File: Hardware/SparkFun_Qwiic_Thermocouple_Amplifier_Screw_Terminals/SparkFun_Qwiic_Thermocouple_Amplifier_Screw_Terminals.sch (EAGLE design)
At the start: 26 parts, among them J1 PTH, U16 MCP9600-SMD

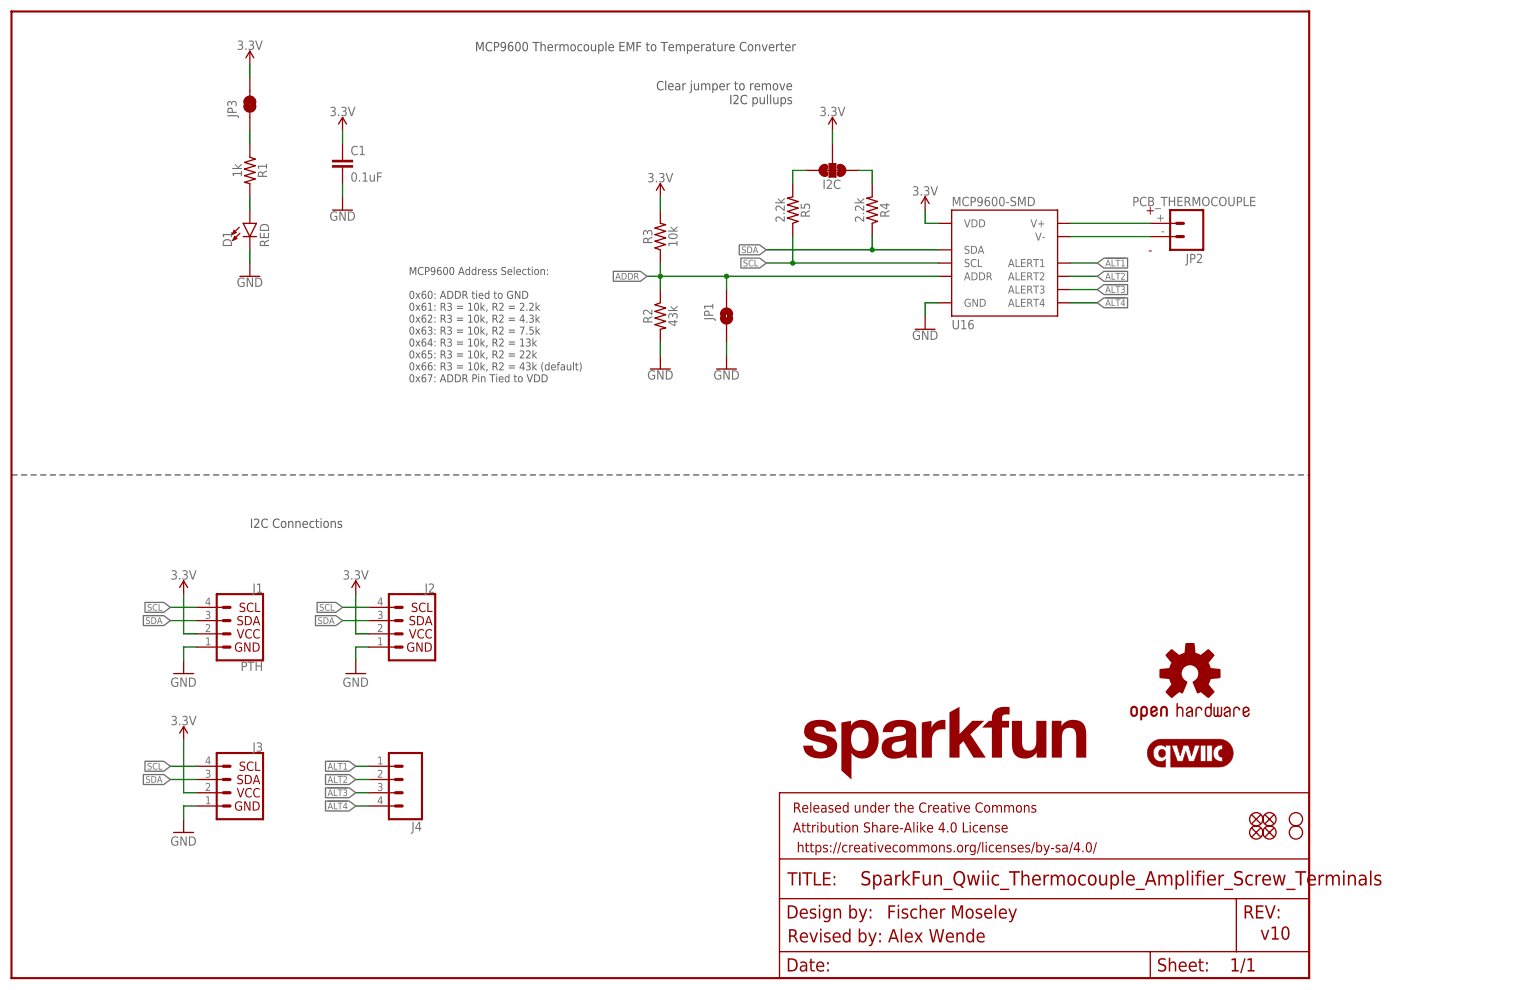
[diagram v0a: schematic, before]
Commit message: Added screw terminal board
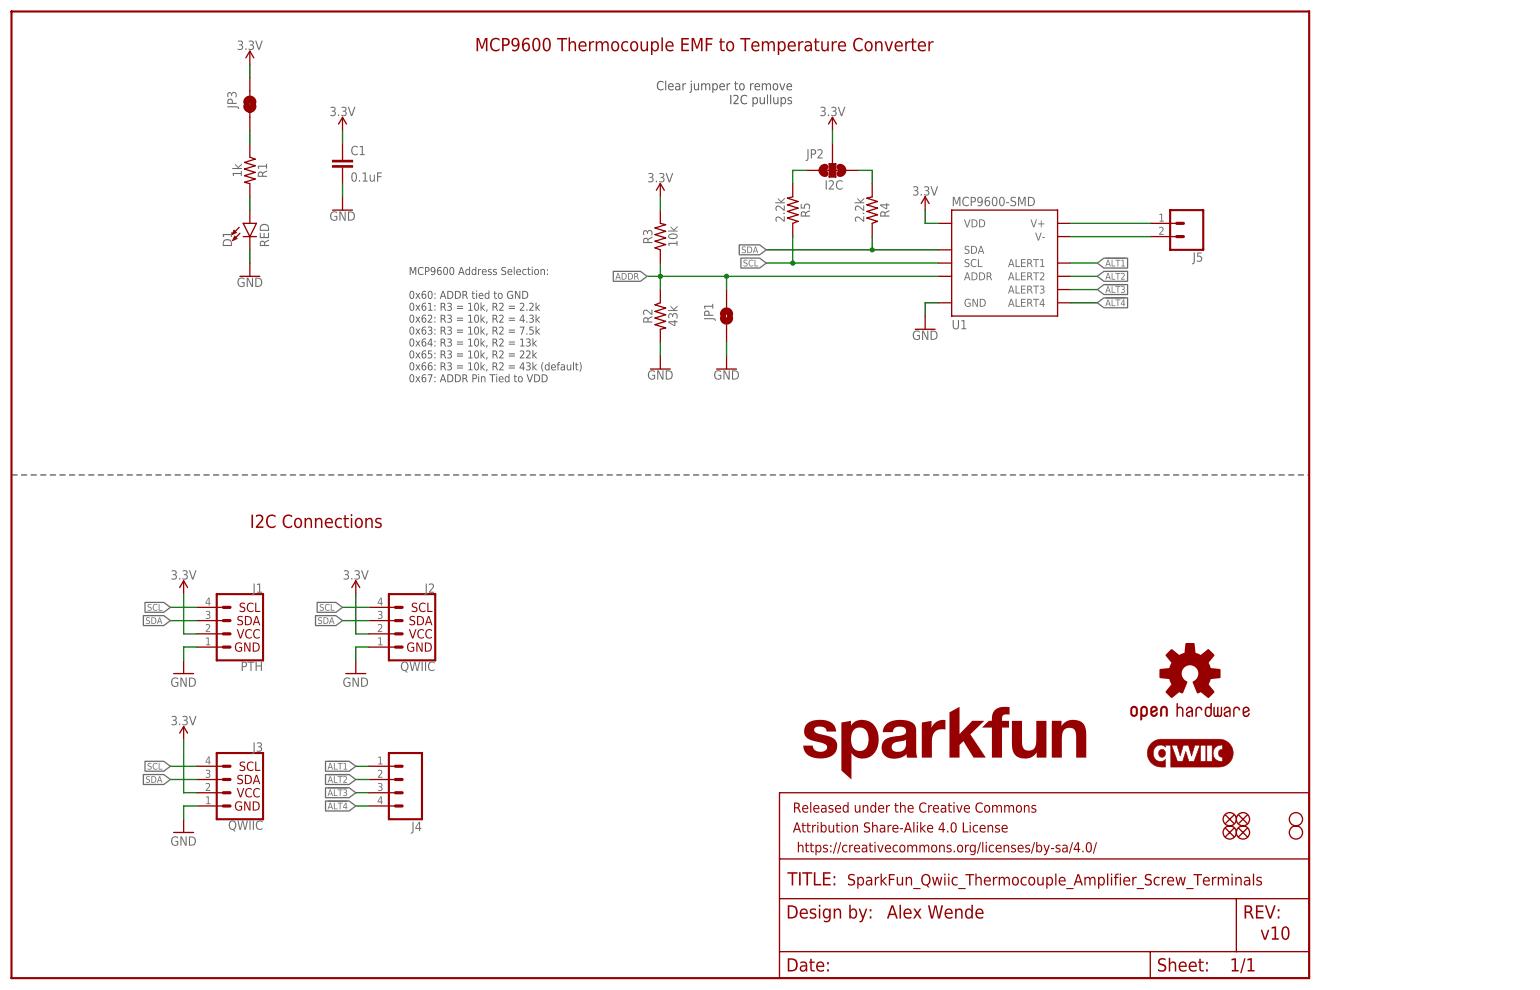
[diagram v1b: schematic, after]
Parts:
- removed I2C: JUMPER-SMT_3_2-NC_TRACE_SILK, SparkFun-Jumpers:JUMPER-SMT_3_2-NC_TRACE_SILK
- removed U16: MCP9600-SMD, MCP9600:MCP9600-SMD
- added J5: (no value), SparkFun-Connectors:CONN_023.5MM
- added U1: MCP9600-SMD, SparkFun-IC-Conversion:MCP9600-SMD
- FD1, FD2, FD3, FD4: value FIDUCIAL1X2 -> FIDUCIALUFIDUCIAL; device SparkFun-Aesthetics:FIDUCIAL1X2 -> SparkFun-Aesthetics:FIDUCIALUFIDUCIAL
- J1: device SparkX:I2C_STANDARD_NO_SILK -> SparkFun-Connectors:I2C_STANDARD_NO_SILK
- J2, J3: value (none) -> QWIIC
- JP2: value PCB_THERMOCOUPLE -> I2C; device MCP9600:PCB_THERMOCOUPLE -> SparkFun-Jumpers:JUMPER-SMT_3_2-NC_TRACE_SILK
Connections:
- net !ALT1: now also U1.ALERT1; no longer U16.ALERT1
- net !ALT2: now also U1.ALERT2; no longer U16.ALERT2
- net !ALT3: now also U1.ALERT3; no longer U16.ALERT3
- net !ALT4: now also U1.ALERT4; no longer U16.ALERT4
- net 3.3V: now also J1.2, JP2.2, JP3.1, U1.VDD; no longer I2C.2, J1.VCC, JP3.2, U16.VDD
- net ADDR: now also U1.ADDR; no longer U16.ADDR
- net GND: now also J1.1, U1.GND; no longer J1.GND, U16.GND
- net N$2: now also JP2.1; no longer I2C.1
- net N$3: now also JP2.3; no longer I2C.3
- net N$4: now also J5.1, U1.V+; no longer JP2G$1.+, U16.V+
- net N$5: now also J5.2, U1.V-; no longer JP2G$1.-, U16.V-
- net N$6: now also JP3.2; no longer JP3.1
- net SCL: now also J1.4, U1.SCL; no longer J1.SCL, U16.SCL
- net SDA: now also J1.3, U1.SDA; no longer J1.SDA, U16.SDA
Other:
- note added: "Alex Wende"
- note removed: "Fischer Moseley"
- note removed: "Revised by: Alex Wende"
- moved on the sheet: JP3

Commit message: Design review changes
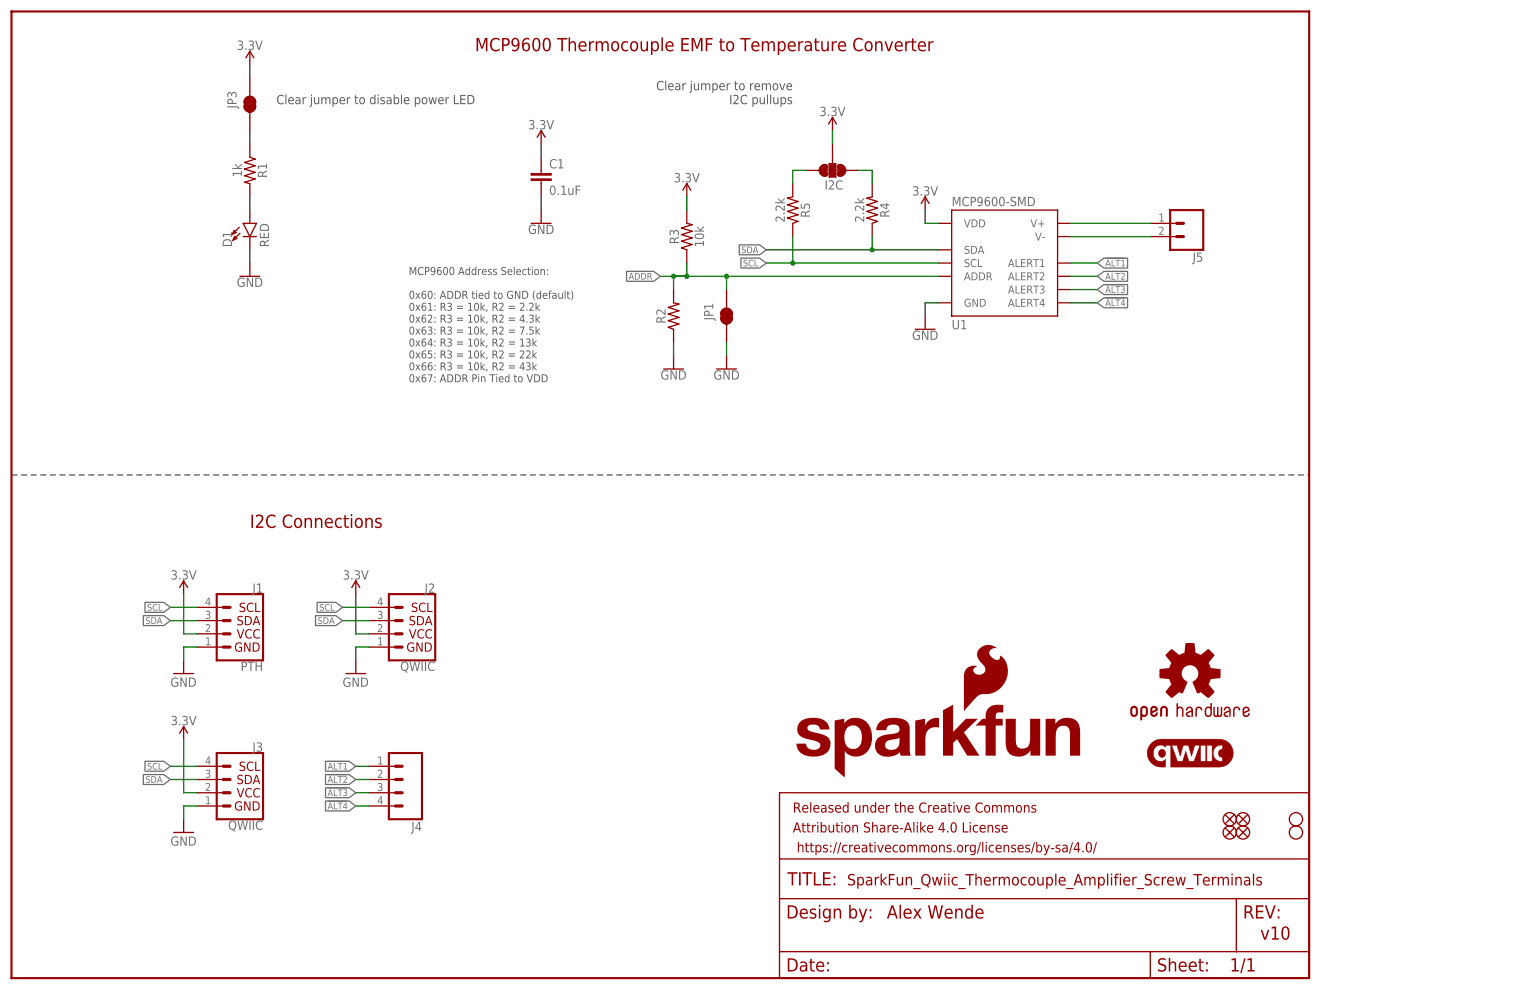
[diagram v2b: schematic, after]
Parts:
- JP1: value JUMPER-SMT_2_NO_SILK -> JUMPER-SMT_2_NC_TRACE_SILK; device SparkFun-Jumpers:JUMPER-SMT_2_NO_SILK -> SparkFun-Jumpers:JUMPER-SMT_2_NC_TRACE_SILK
- LOGO2: value SFE_LOGO_NAME.1_INCH -> SFE_LOGO_NAME_FLAME.1_INCH; device SparkFun-Aesthetics:SFE_LOGO_NAME.1_INCH -> SparkFun-Aesthetics:SFE_LOGO_NAME_FLAME.1_INCH
- R2: value 43k -> (none); device SparkFun-Resistors:43KOHM-0603-1/10W-1% -> SparkFun-Resistors:RESISTORAXIAL-0.3-KIT
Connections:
- net ADDR: now also R2.2; no longer R2.1
- net GND: now also R2.1; no longer R2.2
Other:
- note added: "Clear jumper to disable power LED"
- note added: "MCP9600 Address Selection: 0x60: ADDR tied to GND (default) 0x61: R3 = 10k, R2 = 2.2k 0x62: R3 = 10k, R2 = 4.3k 0x63: R3 = 10k, R2 = 7.5k 0x64: R3 = 10k, R2 = 13k 0x65: R3 = 10k, R2 = 22k 0x66: R3 = 10k, R2 = 43k 0x67: ADDR Pin Tied to VDD"
- note removed: "MCP9600 Address Selection: 0x60: ADDR tied to GND 0x61: R3 = 10k, R2 = 2.2k 0x62: R3 = 10k, R2 = 4.3k 0x63: R3 = 10k, R2 = 7.5k 0x64: R3 = 10k, R2 = 13k 0x65: R3 = 10k, R2 = 22k 0x66: R3 = 10k, R2 = 43k (default) 0x67: ADDR Pin Tied to VDD"
- moved on the sheet: C1, R2, R3
